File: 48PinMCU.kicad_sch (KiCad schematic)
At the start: 34 parts, among them J8 SWD_Header, J9 SWD, SW1 Reset, SW2 SW_SPDT, U6 STM32G473CETx, Y1 Crystal

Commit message: voltage sensor cleanup
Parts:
- renumbered D13 to D11, D14 to D12, D15 to D13, R65 to R66, R66 to R67, R67 to R68, R68 to R69, R69 to R70, R70 to R71, R71 to R72, R72 to R73
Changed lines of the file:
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@@
 		(in_pos_files yes)
 		(dnp no)
-		(property "Reference" "R67"
+		(property "Reference" "R68"
 			(at 183.388 154.686 0)
 			(show_name no)
@@
 			(project "PS-PrechargeBoard"
 				(path "/74d17fe6-68d4-4bd7-954a-e2bbb58b1f1e/00a9aff9-854f-4fe5-b1cf-85d3d4e30c03"
-					(reference "R67")
+					(reference "R68")
 					(unit 1)
 				)
@@
 		(dnp no)
 		(fields_autoplaced yes)
-		(property "Reference" "R66"
+		(property "Reference" "R67"
 			(at 180.848 96.0119 0)
 			(show_name no)
@@
 			(project "PS-PrechargeBoard"
 				(path "/74d17fe6-68d4-4bd7-954a-e2bbb58b1f1e/00a9aff9-854f-4fe5-b1cf-85d3d4e30c03"
-					(reference "R66")
+					(reference "R67")
 					(unit 1)
 				)
@@
 		(dnp no)
 		(fields_autoplaced yes)
-		(property "Reference" "D14"
+		(property "Reference" "D12"
 			(at 238.76 101.5999 90)
 			(show_name no)
@@
 			(project "PS-PrechargeBoard"
 				(path "/74d17fe6-68d4-4bd7-954a-e2bbb58b1f1e/00a9aff9-854f-4fe5-b1cf-85d3d4e30c03"
-					(reference "D14")
+					(reference "D12")
 					(unit 1)
 				)
@@
 		(dnp no)
 		(fields_autoplaced yes)
-		(property "Reference" "D13"
+		(property "Reference" "D11"
 			(at 194.31 142.2399 90)
 			(show_name no)
@@
 			(project "PS-PrechargeBoard"
 				(path "/74d17fe6-68d4-4bd7-954a-e2bbb58b1f1e/00a9aff9-854f-4fe5-b1cf-85d3d4e30c03"
-					(reference "D13")
+					(reference "D11")
 					(unit 1)
 				)
@@
 		(in_pos_files yes)
 		(dnp no)
-		(property "Reference" "R68"
+		(property "Reference" "R69"
 			(at 191.008 154.686 0)
 			(show_name no)
@@
 			(project "PS-PrechargeBoard"
 				(path "/74d17fe6-68d4-4bd7-954a-e2bbb58b1f1e/00a9aff9-854f-4fe5-b1cf-85d3d4e30c03"
-					(reference "R68")
+					(reference "R69")
 					(unit 1)
 				)
@@
 		(in_pos_files yes)
 		(dnp no)
-		(property "Reference" "R72"
+		(property "Reference" "R73"
 			(at 259.588 110.236 0)
 			(show_name no)
@@
 			(project "PS-PrechargeBoard"
 				(path "/74d17fe6-68d4-4bd7-954a-e2bbb58b1f1e/00a9aff9-854f-4fe5-b1cf-85d3d4e30c03"
-					(reference "R72")
+					(reference "R73")
 					(unit 1)
 				)
@@
 		(in_pos_files yes)
 		(dnp no)
-		(property "Reference" "R65"
+		(property "Reference" "R66"
 			(at 175.768 154.686 0)
 			(show_name no)
@@
 			(project "PS-PrechargeBoard"
 				(path "/74d17fe6-68d4-4bd7-954a-e2bbb58b1f1e/00a9aff9-854f-4fe5-b1cf-85d3d4e30c03"
-					(reference "R65")
+					(reference "R66")
 					(unit 1)
 				)
@@
 		(dnp no)
 		(fields_autoplaced yes)
-		(property "Reference" "D15"
+		(property "Reference" "D13"
 			(at 261.62 103.1874 90)
 			(show_name no)
@@
 			(project "PS-PrechargeBoard"
 				(path "/74d17fe6-68d4-4bd7-954a-e2bbb58b1f1e/00a9aff9-854f-4fe5-b1cf-85d3d4e30c03"
-					(reference "D15")
+					(reference "D13")
 					(unit 1)
 				)
@@
 		(in_pos_files yes)
 		(dnp no)
-		(property "Reference" "R70"
+		(property "Reference" "R71"
 			(at 226.06 149.225 90)
 			(show_name no)
@@
 			(project "PS-PrechargeBoard"
 				(path "/74d17fe6-68d4-4bd7-954a-e2bbb58b1f1e/00a9aff9-854f-4fe5-b1cf-85d3d4e30c03"
-					(reference "R70")
+					(reference "R71")
 					(unit 1)
 				)
@@
 		(in_pos_files yes)
 		(dnp no)
-		(property "Reference" "R71"
+		(property "Reference" "R72"
 			(at 248.285 101.5999 0)
 			(show_name no)
@@
 			(project "PS-PrechargeBoard"
 				(path "/74d17fe6-68d4-4bd7-954a-e2bbb58b1f1e/00a9aff9-854f-4fe5-b1cf-85d3d4e30c03"
-					(reference "R71")
+					(reference "R72")
 					(unit 1)
 				)
@@
 		(dnp no)
 		(fields_autoplaced yes)
-		(property "Reference" "R69"
+		(property "Reference" "R70"
 			(at 226.06 137.795 90)
 			(show_name no)
@@
 			(project "PS-PrechargeBoard"
 				(path "/74d17fe6-68d4-4bd7-954a-e2bbb58b1f1e/00a9aff9-854f-4fe5-b1cf-85d3d4e30c03"
-					(reference "R69")
+					(reference "R70")
 					(unit 1)
 				)

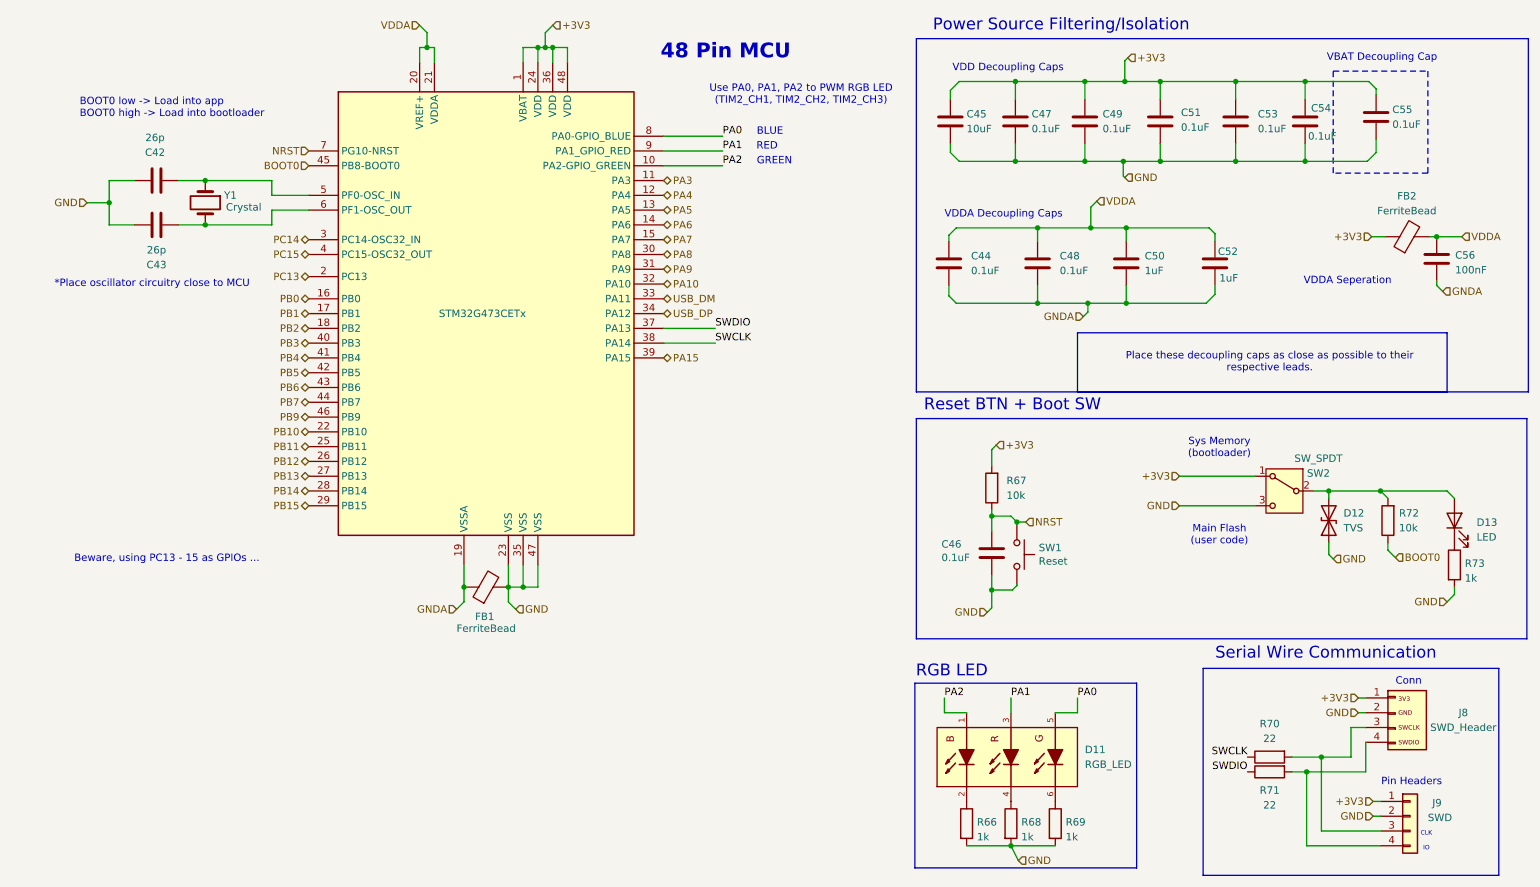
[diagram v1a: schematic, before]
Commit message: updated usb-c connector
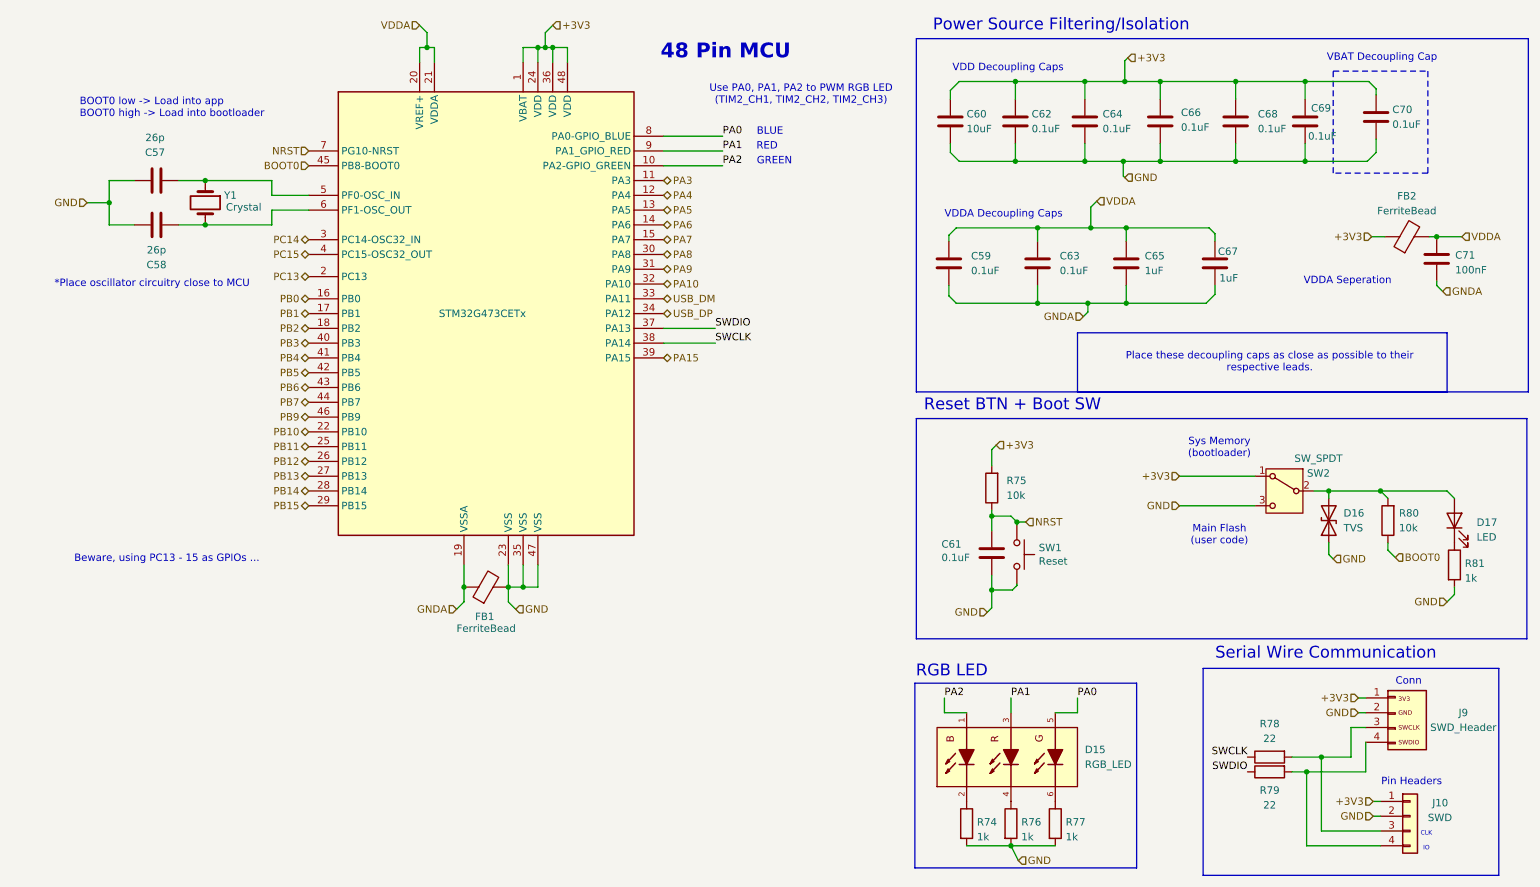
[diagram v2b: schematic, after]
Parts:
- renumbered C42 to C57, C43 to C58, C44 to C59, C45 to C60, C46 to C61, C47 to C62, C48 to C63, C49 to C64, C50 to C65, C51 to C66, C52 to C67, C53 to C68, C54 to C69, C55 to C70, C56 to C71, D11 to D15, D12 to D16, D13 to D17, J9 to J10, J8 to J9, R66 to R74, R67 to R75, R68 to R76, R69 to R77, R70 to R78, R71 to R79, R72 to R80, R73 to R81, U6 to U8
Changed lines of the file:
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@@
 		(dnp no)
 		(fields_autoplaced yes)
-		(property "Reference" "C50"
+		(property "Reference" "C65"
 			(at 204.597 57.4039 0)
 			(show_name no)
@@
 			(project "PS-PrechargeBoard"
 				(path "/74d17fe6-68d4-4bd7-954a-e2bbb58b1f1e/00a9aff9-854f-4fe5-b1cf-85d3d4e30c03"
-					(reference "C50")
+					(reference "C65")
 					(unit 1)
 				)
@@
 		(in_pos_files yes)
 		(dnp no)
-		(property "Reference" "R68"
+		(property "Reference" "R76"
 			(at 183.388 154.686 0)
 			(show_name no)
@@
 			(project "PS-PrechargeBoard"
 				(path "/74d17fe6-68d4-4bd7-954a-e2bbb58b1f1e/00a9aff9-854f-4fe5-b1cf-85d3d4e30c03"
-					(reference "R68")
+					(reference "R76")
 					(unit 1)
 				)
@@
 		(dnp no)
 		(fields_autoplaced yes)
-		(property "Reference" "R67"
+		(property "Reference" "R75"
 			(at 180.848 96.0119 0)
 			(show_name no)
@@
 			(project "PS-PrechargeBoard"
 				(path "/74d17fe6-68d4-4bd7-954a-e2bbb58b1f1e/00a9aff9-854f-4fe5-b1cf-85d3d4e30c03"
-					(reference "R67")
+					(reference "R75")
 					(unit 1)
 				)
@@
 		(dnp no)
 		(fields_autoplaced yes)
-		(property "Reference" "D12"
+		(property "Reference" "D16"
 			(at 238.76 101.5999 90)
 			(show_name no)
@@
 			(project "PS-PrechargeBoard"
 				(path "/74d17fe6-68d4-4bd7-954a-e2bbb58b1f1e/00a9aff9-854f-4fe5-b1cf-85d3d4e30c03"
-					(reference "D12")
+					(reference "D16")
 					(unit 1)
 				)
@@
 		(in_pos_files yes)
 		(dnp no)
-		(property "Reference" "U6"
+		(property "Reference" "U8"
 			(at 88.392 73.66 0)
 			(hide yes)
@@
 			(project "PS-PrechargeBoard"
 				(path "/74d17fe6-68d4-4bd7-954a-e2bbb58b1f1e/00a9aff9-854f-4fe5-b1cf-85d3d4e30c03"
-					(reference "U6")
+					(reference "U8")
 					(unit 1)
 				)
@@
 		(in_pos_files yes)
 		(dnp no)
-		(property "Reference" "J8"
+		(property "Reference" "J9"
 			(at 259.334 135.89 0)
 			(show_name no)
@@
 			(project "PS-PrechargeBoard"
 				(path "/74d17fe6-68d4-4bd7-954a-e2bbb58b1f1e/00a9aff9-854f-4fe5-b1cf-85d3d4e30c03"
-					(reference "J8")
+					(reference "J9")
 					(unit 1)
 				)
@@
 		(in_pos_files yes)
 		(dnp no)
-		(property "Reference" "C55"
+		(property "Reference" "C70"
 			(at 247.142 32.258 0)
 			(show_name no)
@@
 			(project "PS-PrechargeBoard"
 				(path "/74d17fe6-68d4-4bd7-954a-e2bbb58b1f1e/00a9aff9-854f-4fe5-b1cf-85d3d4e30c03"
-					(reference "C55")
+					(reference "C70")
 					(unit 1)
 				)
@@
 		(dnp no)
 		(fields_autoplaced yes)
-		(property "Reference" "C48"
+		(property "Reference" "C63"
 			(at 189.992 57.4039 0)
 			(show_name no)
@@
 			(project "PS-PrechargeBoard"
 				(path "/74d17fe6-68d4-4bd7-954a-e2bbb58b1f1e/00a9aff9-854f-4fe5-b1cf-85d3d4e30c03"
-					(reference "C48")
+					(reference "C63")
 					(unit 1)
 				)
@@
 		(in_pos_files yes)
 		(dnp no)
-		(property "Reference" "C47"
+		(property "Reference" "C62"
 			(at 185.166 33.02 0)
 			(show_name no)
@@
 			(project "PS-PrechargeBoard"
 				(path "/74d17fe6-68d4-4bd7-954a-e2bbb58b1f1e/00a9aff9-854f-4fe5-b1cf-85d3d4e30c03"
-					(reference "C47")
+					(reference "C62")
 					(unit 1)
 				)
@@
 		(dnp no)
 		(fields_autoplaced yes)
-		(property "Reference" "C44"
+		(property "Reference" "C59"
 			(at 174.752 57.4039 0)
 			(show_name no)
@@
 			(project "PS-PrechargeBoard"
 				(path "/74d17fe6-68d4-4bd7-954a-e2bbb58b1f1e/00a9aff9-854f-4fe5-b1cf-85d3d4e30c03"
-					(reference "C44")
+					(reference "C59")
 					(unit 1)
 				)
@@
 		(dnp no)
 		(fields_autoplaced yes)
-		(property "Reference" "C56"
+		(property "Reference" "C71"
 			(at 257.937 57.277 0)
 			(show_name no)
@@
 			(project "PS-PrechargeBoard"
 				(path "/74d17fe6-68d4-4bd7-954a-e2bbb58b1f1e/00a9aff9-854f-4fe5-b1cf-85d3d4e30c03"
-					(reference "C56")
+					(reference "C71")
 					(unit 1)
 				)
@@
 		(in_pos_files yes)
 		(dnp no)
-		(property "Reference" "C51"
+		(property "Reference" "C66"
 			(at 210.82 32.766 0)
 			(show_name no)
@@
 			(project "PS-PrechargeBoard"
 				(path "/74d17fe6-68d4-4bd7-954a-e2bbb58b1f1e/00a9aff9-854f-4fe5-b1cf-85d3d4e30c03"
-					(reference "C51")
+					(reference "C66")
 					(unit 1)
 				)
@@
 		(dnp no)
 		(fields_autoplaced yes)
-		(property "Reference" "C53"
+		(property "Reference" "C68"
 			(at 224.028 33.0199 0)
 			(show_name no)
@@
 			(project "PS-PrechargeBoard"
 				(path "/74d17fe6-68d4-4bd7-954a-e2bbb58b1f1e/00a9aff9-854f-4fe5-b1cf-85d3d4e30c03"
-					(reference "C53")
+					(reference "C68")
 					(unit 1)
 				)
@@
 		(dnp no)
 		(fields_autoplaced yes)
-		(property "Reference" "D11"
+		(property "Reference" "D15"
 			(at 194.31 142.2399 90)
 			(show_name no)
@@
 			(project "PS-PrechargeBoard"
 				(path "/74d17fe6-68d4-4bd7-954a-e2bbb58b1f1e/00a9aff9-854f-4fe5-b1cf-85d3d4e30c03"
-					(reference "D11")
+					(reference "D15")
 					(unit 1)
 				)
@@
 		(in_pos_files yes)
 		(dnp no)
-		(property "Reference" "R69"
+		(property "Reference" "R77"
 			(at 191.008 154.686 0)
 			(show_name no)
@@
 			(project "PS-PrechargeBoard"
 				(path "/74d17fe6-68d4-4bd7-954a-e2bbb58b1f1e/00a9aff9-854f-4fe5-b1cf-85d3d4e30c03"
-					(reference "R69")
+					(reference "R77")
 					(unit 1)
 				)
@@
 		(in_pos_files yes)
 		(dnp no)
-		(property "Reference" "R73"
+		(property "Reference" "R81"
 			(at 259.588 110.236 0)
 			(show_name no)
@@
 			(project "PS-PrechargeBoard"
 				(path "/74d17fe6-68d4-4bd7-954a-e2bbb58b1f1e/00a9aff9-854f-4fe5-b1cf-85d3d4e30c03"
-					(reference "R73")
+					(reference "R81")
 					(unit 1)
 				)
@@
 		(in_pos_files yes)
 		(dnp no)
-		(property "Reference" "C42"
+		(property "Reference" "C57"
 			(at 34.544 39.624 90)
 			(show_name no)
@@
 			(project "PS-PrechargeBoard"
 				(path "/74d17fe6-68d4-4bd7-954a-e2bbb58b1f1e/00a9aff9-854f-4fe5-b1cf-85d3d4e30c03"
-					(reference "C42")
+					(reference "C57")
 					(unit 1)
 				)
@@
 		(in_pos_files yes)
 		(dnp no)
-		(property "Reference" "C45"
+		(property "Reference" "C60"
 			(at 173.99 33.02 0)
 			(show_name no)
@@
 			(project "PS-PrechargeBoard"
 				(path "/74d17fe6-68d4-4bd7-954a-e2bbb58b1f1e/00a9aff9-854f-4fe5-b1cf-85d3d4e30c03"
-					(reference "C45")
+					(reference "C60")
 					(unit 1)
 				)
@@
 		(in_pos_files yes)
 		(dnp no)
-		(property "Reference" "R66"
+		(property "Reference" "R74"
 			(at 175.768 154.686 0)
 			(show_name no)
@@
 			(project "PS-PrechargeBoard"
 				(path "/74d17fe6-68d4-4bd7-954a-e2bbb58b1f1e/00a9aff9-854f-4fe5-b1cf-85d3d4e30c03"
-					(reference "R66")
+					(reference "R74")
 					(unit 1)
 				)
@@
 		(dnp no)
 		(fields_autoplaced yes)
-		(property "Reference" "D13"
+		(property "Reference" "D17"
 			(at 261.62 103.1874 90)
 			(show_name no)
@@
 			(project "PS-PrechargeBoard"
 				(path "/74d17fe6-68d4-4bd7-954a-e2bbb58b1f1e/00a9aff9-854f-4fe5-b1cf-85d3d4e30c03"
-					(reference "D13")
+					(reference "D17")
 					(unit 1)
 				)
@@
 		(in_pos_files yes)
 		(dnp no)
-		(property "Reference" "C52"
+		(property "Reference" "C67"
 			(at 217.17 56.642 0)
 			(show_name no)
@@
 			(project "PS-PrechargeBoard"
 				(path "/74d17fe6-68d4-4bd7-954a-e2bbb58b1f1e/00a9aff9-854f-4fe5-b1cf-85d3d4e30c03"
-					(reference "C52")
+					(reference "C67")
 					(unit 1)
 				)
@@
 		(in_pos_files yes)
 		(dnp no)
-		(property "Reference" "R71"
+		(property "Reference" "R79"
 			(at 226.06 149.225 90)
 			(show_name no)
@@
 			(project "PS-PrechargeBoard"
 				(path "/74d17fe6-68d4-4bd7-954a-e2bbb58b1f1e/00a9aff9-854f-4fe5-b1cf-85d3d4e30c03"
-					(reference "R71")
+					(reference "R79")
 					(unit 1)
 				)
@@
 		(in_pos_files yes)
 		(dnp no)
-		(property "Reference" "C46"
+		(property "Reference" "C61"
 			(at 169.672 106.934 0)
 			(show_name no)
@@
 			(project "PS-PrechargeBoard"
 				(path "/74d17fe6-68d4-4bd7-954a-e2bbb58b1f1e/00a9aff9-854f-4fe5-b1cf-85d3d4e30c03"
-					(reference "C46")
+					(reference "C61")
 					(unit 1)
 				)
@@
 		(in_pos_files yes)
 		(dnp no)
-		(property "Reference" "R72"
+		(property "Reference" "R80"
 			(at 248.285 101.5999 0)
 			(show_name no)
@@
 			(project "PS-PrechargeBoard"
 				(path "/74d17fe6-68d4-4bd7-954a-e2bbb58b1f1e/00a9aff9-854f-4fe5-b1cf-85d3d4e30c03"
-					(reference "R72")
+					(reference "R80")
 					(unit 1)
 				)
@@
 		(in_pos_files yes)
 		(dnp no)
-		(property "Reference" "C49"
+		(property "Reference" "C64"
 			(at 197.358 33.02 0)
 			(show_name no)
@@
 			(project "PS-PrechargeBoard"
 				(path "/74d17fe6-68d4-4bd7-954a-e2bbb58b1f1e/00a9aff9-854f-4fe5-b1cf-85d3d4e30c03"
-					(reference "C49")
+					(reference "C64")
 					(unit 1)
 				)
@@
 		(in_pos_files yes)
 		(dnp no)
-		(property "Reference" "J9"
+		(property "Reference" "J10"
 			(at 254 151.384 0)
 			(show_name no)
@@
 			(project "PS-PrechargeBoard"
 				(path "/74d17fe6-68d4-4bd7-954a-e2bbb58b1f1e/00a9aff9-854f-4fe5-b1cf-85d3d4e30c03"
-					(reference "J9")
+					(reference "J10")
 					(unit 1)
 				)
@@
 		(dnp no)
 		(fields_autoplaced yes)
-		(property "Reference" "C43"
+		(property "Reference" "C58"
 			(at 34.798 58.928 90)
 			(show_name no)
@@
 			(project "PS-PrechargeBoard"
 				(path "/74d17fe6-68d4-4bd7-954a-e2bbb58b1f1e/00a9aff9-854f-4fe5-b1cf-85d3d4e30c03"
-					(reference "C43")
+					(reference "C58")
 					(unit 1)
 				)
@@
 		(dnp no)
 		(fields_autoplaced yes)
-		(property "Reference" "R70"
+		(property "Reference" "R78"
 			(at 226.06 137.795 90)
 			(show_name no)
@@
 			(project "PS-PrechargeBoard"
 				(path "/74d17fe6-68d4-4bd7-954a-e2bbb58b1f1e/00a9aff9-854f-4fe5-b1cf-85d3d4e30c03"
-					(reference "R70")
+					(reference "R78")
 					(unit 1)
 				)
@@
 		(in_pos_files yes)
 		(dnp no)
-		(property "Reference" "C54"
+		(property "Reference" "C69"
 			(at 233.172 32.004 0)
 			(show_name no)
@@
 			(project "PS-PrechargeBoard"
 				(path "/74d17fe6-68d4-4bd7-954a-e2bbb58b1f1e/00a9aff9-854f-4fe5-b1cf-85d3d4e30c03"
-					(reference "C54")
+					(reference "C69")
 					(unit 1)
 				)
